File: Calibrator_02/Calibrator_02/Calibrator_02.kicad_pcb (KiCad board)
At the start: 2 copper layers, 100 x 50 mm, 88 parts, among them J1 Conn_01x04, J2 DB9_Female_MountingHoles, J3 Conn_Coaxial, J5 Conn_01x01_Female, J6 Conn_01x04, M1 AW9523BTQR, U1 KAQY214STLD, U10 KAQY214STLD, U11 KAQY214STLD, U12 KAQY214STLD, U13 KAQY214STLD, U14 KAQY214STLD, U15 KAQY214STLD, U16 KAQY214STLD, U17 KAQY214STLD, U18 KAQY214STLD, U19 KAQY214STLD, U2 KAQY214STLD, U20 KAQY214STLD, U21 KAQY214STLD, U22 KAQY214STLD, U23 KAQY214STLD, U24 KAQY214STLD, U25 KAQY214STLD, U26 KAQY214STLD, U27 KAQY214STLD, U28 KAQY214STLD, U29 KAQY214STLD, U3 KAQY214STLD, U30 KAQY214STLD, U31 KAQY214STLD, U32 KAQY214STLD, U4 KAQY214STLD, U5 KAQY214STLD, U6 KAQY214STLD, U7 KAQY214STLD, U8 KAQY214STLD, U9 KAQY214STLD

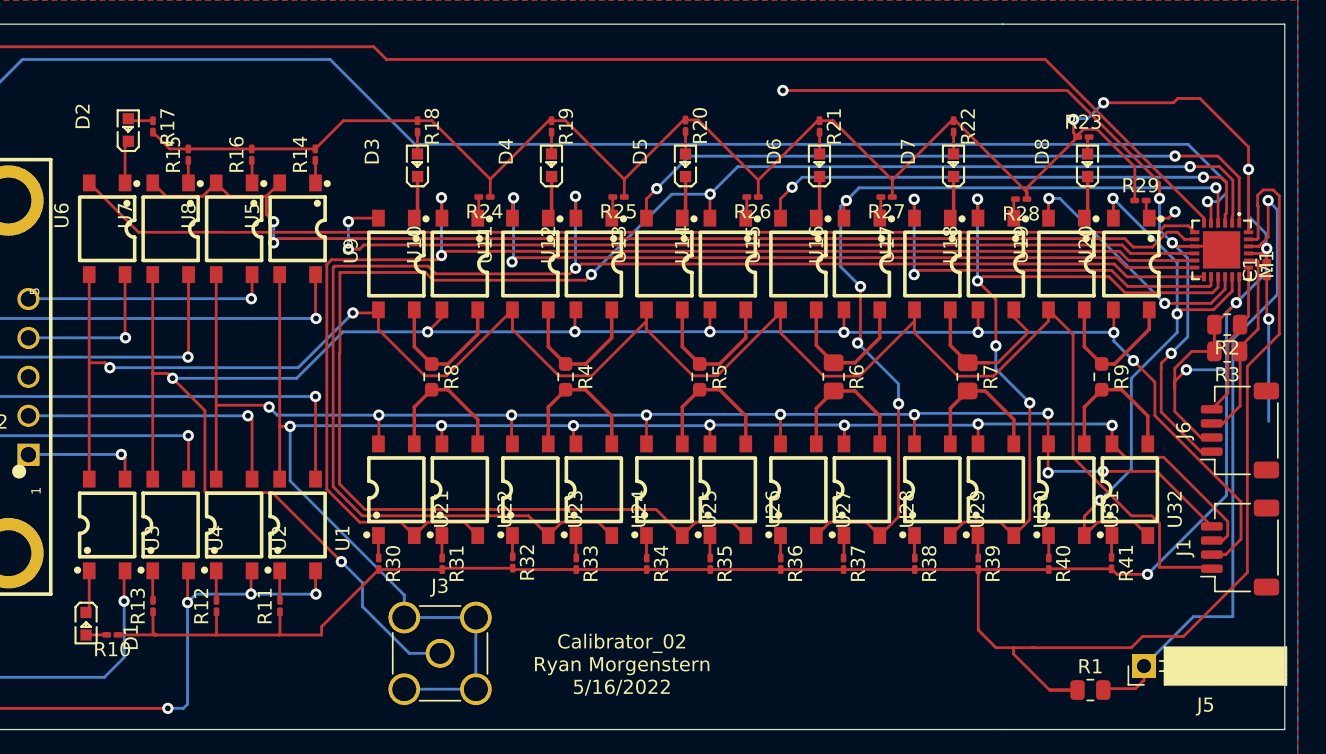
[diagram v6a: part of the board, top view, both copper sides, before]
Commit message: Fixed footprint
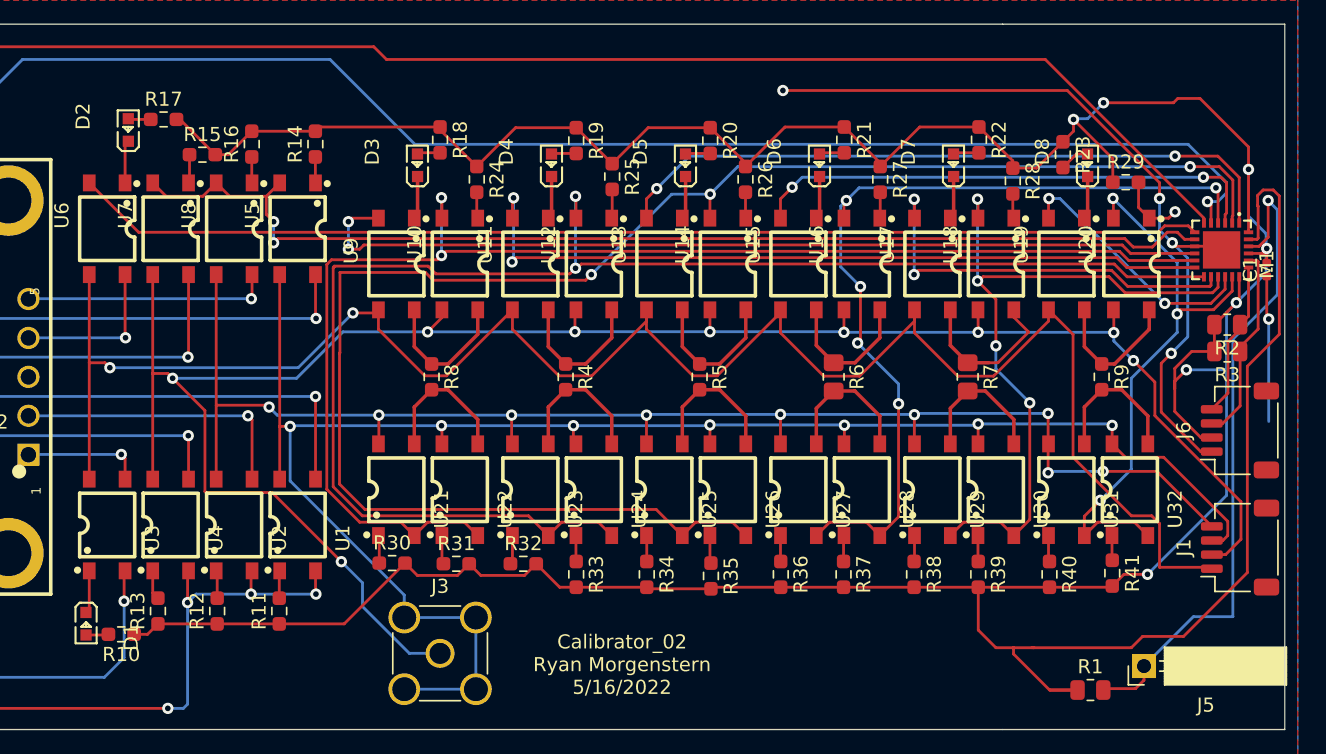
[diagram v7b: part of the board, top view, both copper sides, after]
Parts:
- R10, R11, R12, R13, R14, R15, R16, R17, R18, R19, R20, R21, R22, R23, R24, R25, R26, R27, R28, R29, R30, R31, R32, R33, R34, R35, R36, R37, R38, R39, R40, R41: footprint Resistor_SMD:R_0201_0603Metric_Pad0.64x0.40mm_HandSolder -> Resistor_SMD:R_0603_1608Metric_Pad0.98x0.95mm_HandSolder
- moved R20 2.04 mm to (49.8, -16.8)
- moved R22 2.04 mm to (68.8, -16.8)
- moved R19 2.02 mm to (40.2, -16.8)
- moved R21 1.99 mm to (59.2, -16.8)
- moved R23 1.91 mm to (74.8, -15.8), turned to 270 degrees
- moved R18 1.86 mm to (30.6, -16.8)
- moved R29 1.67 mm to (79.2, -13.8)
- moved R25 1.52 mm to (42.8, -14.2), turned to 270 degrees
- moved R28 1.42 mm to (71.2, -13.9), turned to 270 degrees
- moved R24 1.37 mm to (33.2, -14.0), turned to 270 degrees
- moved R26 1.35 mm to (52.2, -14.0), turned to 270 degrees
- moved R27 1.33 mm to (61.8, -14.0), turned to 270 degrees
- moved R15 1.00 mm to (13.8, -15.8), turned to 0 degrees
- moved R31 1.00 mm to (31.8, 13.2), turned to 0 degrees
- moved R30 0.95 mm to (27.2, 13.2), turned to 0 degrees
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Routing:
- net +3V3: track 324.6 -> 303.0 mm
- net Net-(R29-Pad2): track 3.84 -> 5.67 mm
- net Net-(D8-Pad2): track 1.25 -> 2.15 mm
- net Net-(R25-Pad2): track 1.81 -> 2.43 mm
- net Net-(R32-Pad1): track 1.51 -> 2.06 mm
